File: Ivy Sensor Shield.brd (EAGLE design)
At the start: 47.1 x 37.2 mm, 16 parts

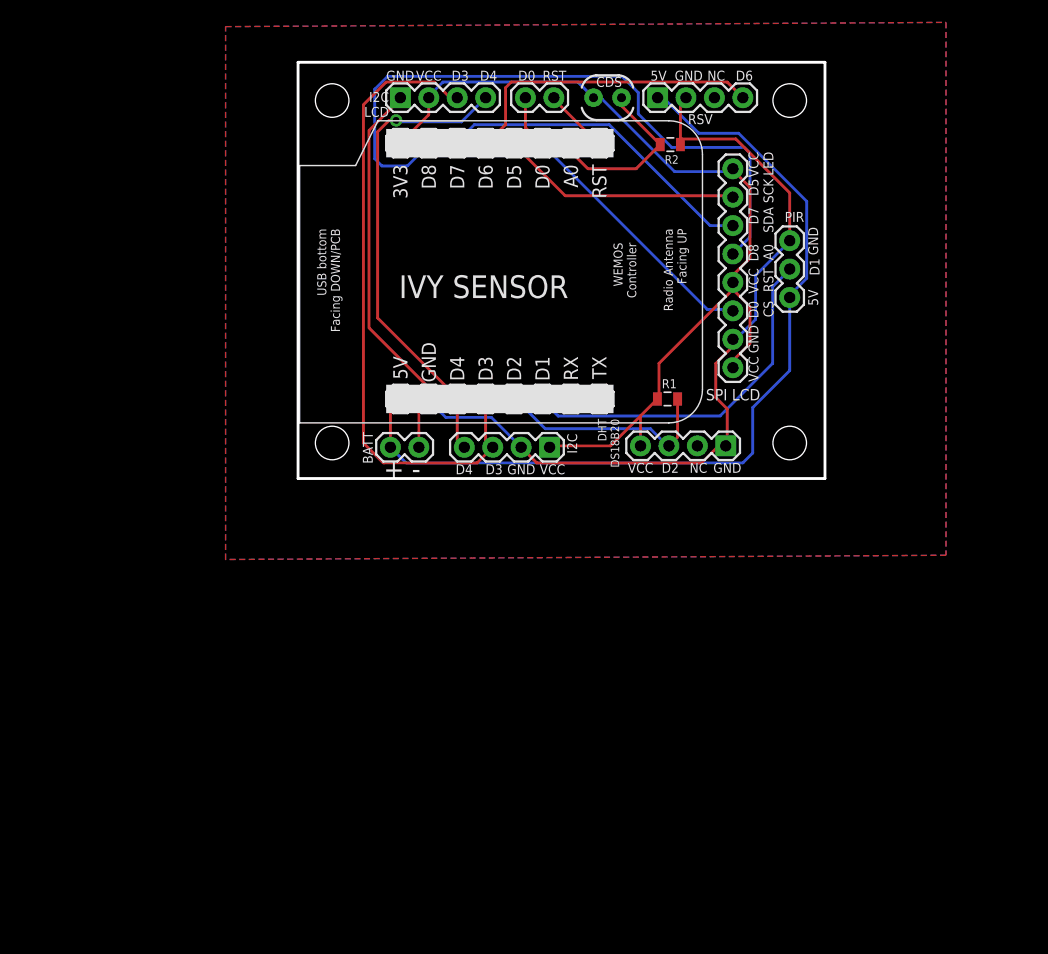
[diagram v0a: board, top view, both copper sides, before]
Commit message: Update Sensor to version 0.2
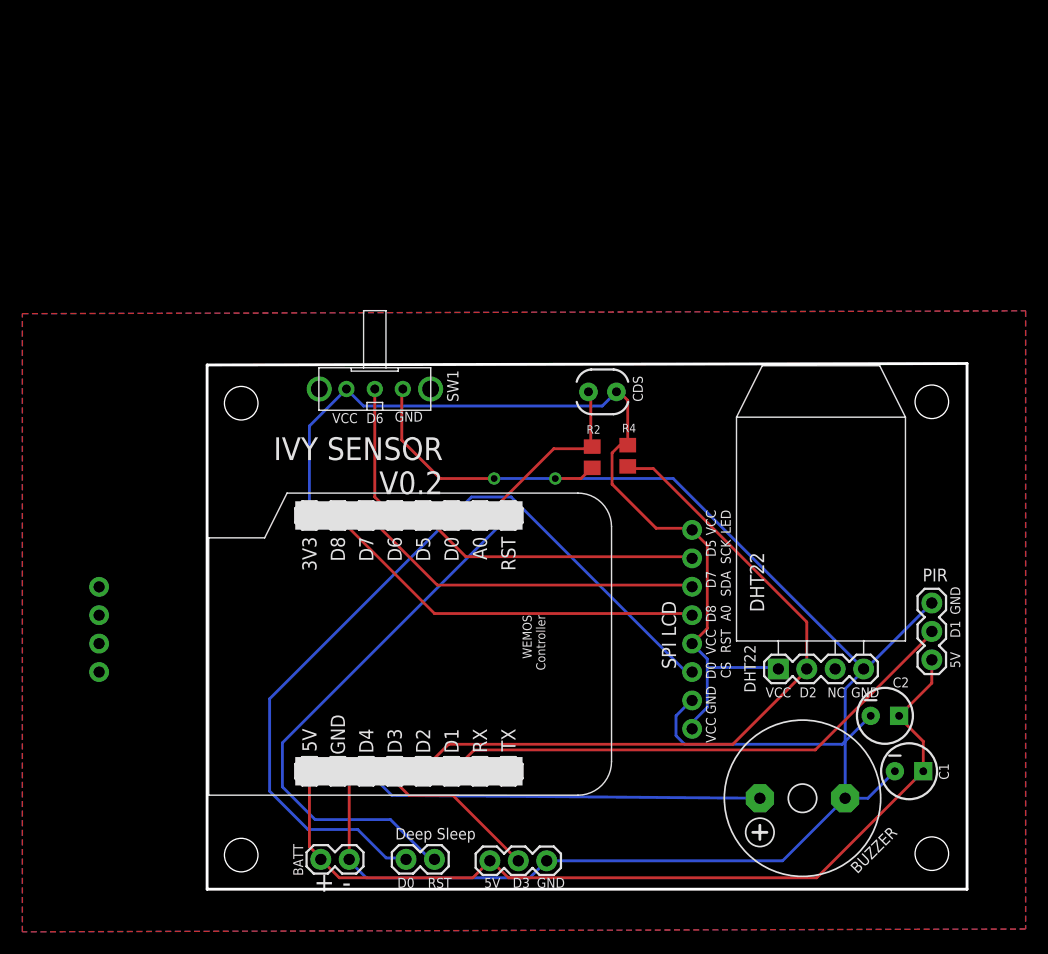
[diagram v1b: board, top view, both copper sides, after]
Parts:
- removed DHT_DS18B20, I2C_OLED: (no value), SparkFun-Connectors:1X04
- removed I2C: I2C, SparkFun-Connectors:1X04
- removed R1: 4.7K, SparkFun-Passives:0805
- removed SPI_TFT: (no value), SparkFun-Connectors:1X08_ROUND
- added BUZZER: F/CM12P, buzzer:F/CM12P
- added C1: 47uF/16V, SparkFun-Capacitors:CPOL-RADIAL-10UF-25V
- added C2: 102pF, SparkFun-Capacitors:CPOL-RADIAL-10UF-25V
- added DHT22: (no value), RHT03_DHT-22_AM2302:RHT03_DHT-22/RA
- added R4: 4.7K, resistor:R0805
- added SW1: OS102011MA1Q, adafruit:OS102011MA1Q
- added TFT_LCD: 1.8"_TFT, tft_1.8_1.44_oled_0.96:1.8"_TFT
- R2: device SparkFun-Passives:0805 -> resistor:R0805
- RSV: value (none) -> Reserved; device SparkFun-Connectors:1X04 -> SparkFun-Connectors:1X03
- moved RSV 69.8 mm to (43.3, 6.86)
- moved DEEP_SLEEP_JP 68.9 mm to (38.4, 6.99)
- moved U$7 38.8 mm to (82.8, 7.49)
- moved U$6 37.7 mm to (21.1, 7.37)
- moved BATT 37.4 mm to (30.7, 6.99)
- moved PIR 34.8 mm to (82.8, 24.8)
- moved U$2 34.3 mm to (27.2, 37.7)
- moved U$8 29.8 mm to (82.8, 47.9)
- moved R2 28.8 mm to (52.5, 42.9), turned to 270 degrees
- moved U$9 28.2 mm to (21.1, 47.8)
- moved R3 26.3 mm to (53.5, 48.8), turned to 180 degrees
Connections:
- removed net NC: DHT_DS18B20.2
- removed net NC2: RSV.3
- net 5V: now also C1.1, C2.1
- net D0: now also TFT_LCD.P$14; no longer SPI_TFT.6
- net D2: now also DHT22.DATA, R4.2; no longer DHT_DS18B20.3, R1.1
- net D3: now also RSV.2; no longer I2C.3, I2C_OLED.3
- net D4: now also BUZZER.+; no longer I2C.4, I2C_OLED.4
- net D5: now also TFT_LCD.P$10; no longer SPI_TFT.2
- net D6: now also SW1.2; no longer RSV.4
- net D7: now also TFT_LCD.P$11; no longer SPI_TFT.3
- net D8: now also TFT_LCD.P$12; no longer SPI_TFT.4
- net GND: now also BUZZER.-, C1.2, C2.2, DHT22.GND, RSV.3, SW1.1, TFT_LCD.P$15; no longer DHT_DS18B20.1, I2C.2, I2C_OLED.1, RSV.2, SPI_TFT.7
- net VCC: now also DHT22.VDD, R4.1, SW1.3, TFT_LCD.P$13, TFT_LCD.P$16, TFT_LCD.P$9; no longer DHT_DS18B20.4, I2C.1, I2C_OLED.2, R1.2, SPI_TFT.1, SPI_TFT.5, SPI_TFT.8
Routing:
- net GND: track 107.1 -> 163.5 mm, vias 0 -> 2
- net D0: track 28.1 -> 74.8 mm
- net D2: track 20.1 -> 64.2 mm
- net RST: track 5.87 -> 48.8 mm
- net D3: track 57.4 -> 14.8 mm
- net D8: track 59.7 -> 35.3 mm
- net D1: track 32.2 -> 48.3 mm
- net D6: track 27.8 -> 12.2 mm
- net D4: track 42.8 -> 36.1 mm, vias 1 -> 0
- net D5: track 21.8 -> 25.7 mm
- net D7: track 29.1 -> 31.8 mm
- net A0: track 16.2 -> 17.7 mm
- net VCC: track 83.6 -> 83.0 mm
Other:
- board size 47.1 x 37.2 mm -> 67.9 x 47 mm
- board text added: "DHT22"
- board text added: "Deep Sleep"
- board text added: "IVY SENSOR V0.2"
- board text removed: "D4"
- board text removed: "DHT DS18B20"
- board text removed: "I2C LCD"
- board text removed: "IVY SENSOR"
